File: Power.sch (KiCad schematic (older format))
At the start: 3 parts, among them P1 CONN_02X10, P2 CONN_01X05, P3 CONN_01X02

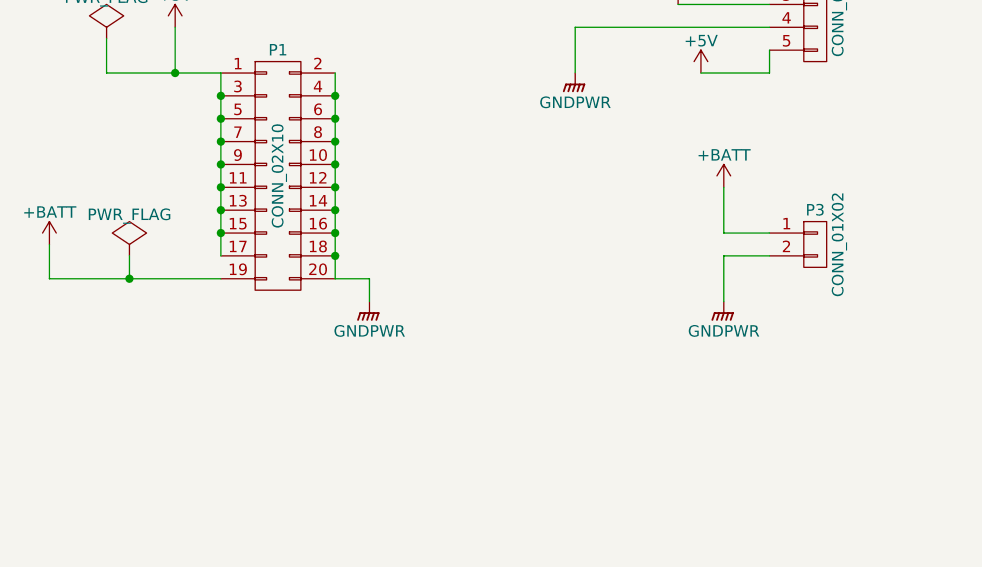
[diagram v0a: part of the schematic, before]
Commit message: Add voltage divider to pololu power
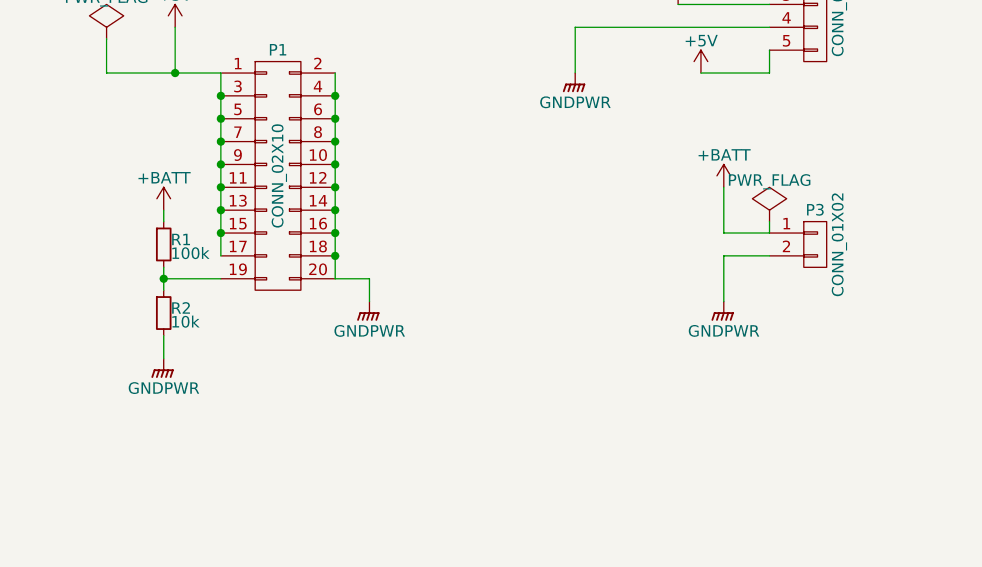
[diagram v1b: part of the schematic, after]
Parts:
- added R1: 100k, Resistors_SMD:R_0603_HandSoldering, symbol R_Small
- added R2: 10k, Resistors_SMD:R_0603_HandSoldering, symbol R_Small
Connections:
- net +BATT: now also R1.1; no longer P1.19 (P19)
- net GNDPWR: now also R2.2
- new net: P1.19 (P19), R1.2, R2.1
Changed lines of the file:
@@
 $EndComp
 $Comp
-L +BATT #PWR01
-U 1 1 56443E57
-P 650 4050
-F 0 "#PWR01" H 650 3900 50  0001 C CNN
-F 1 "+BATT" H 650 4190 50  0000 C CNN
-F 2 "" H 650 4050 60  0000 C CNN
-F 3 "" H 650 4050 60  0000 C CNN
-	1    650  4050
-	1    0    0    -1
-$EndComp
-Wire Wire Line
-	1400 4200 650  4200
-Wire Wire Line
-	650  4200 650  4050
+L GNDPWR #PWR01
+U 1 1 56443ECC
+P 2050 4300
+F 0 "#PWR01" H 2050 4100 50  0001 C CNN
+F 1 "GNDPWR" H 2050 4170 50  0000 C CNN
+F 2 "" H 2050 4250 60  0000 C CNN
+F 3 "" H 2050 4250 60  0000 C CNN
+	1    2050 4300
+	1    0    0    -1
+$EndComp
+$Comp
+L +5V #PWR02
+U 1 1 56443FAD
+P 1200 3100
+F 0 "#PWR02" H 1200 2950 50  0001 C CNN
+F 1 "+5V" H 1200 3240 50  0000 C CNN
+F 2 "" H 1200 3100 60  0000 C CNN
+F 3 "" H 1200 3100 60  0000 C CNN
+	1    1200 3100
+	1    0    0    -1
+$EndComp
+$Comp
+L PWR_FLAG #FLG03
+U 1 1 56443FC4
+P 3800 3950
+F 0 "#FLG03" H 3800 4045 50  0001 C CNN
+F 1 "PWR_FLAG" H 3800 4130 50  0000 C CNN
+F 2 "" H 3800 3950 60  0000 C CNN
+F 3 "" H 3800 3950 60  0000 C CNN
+	1    3800 3950
+	1    0    0    -1
+$EndComp
+$Comp
+L PWR_FLAG #FLG04
+U 1 1 56443FEA
+P 900 3150
+F 0 "#FLG04" H 900 3245 50  0001 C CNN
+F 1 "PWR_FLAG" H 900 3330 50  0000 C CNN
+F 2 "" H 900 3150 60  0000 C CNN
+F 3 "" H 900 3150 60  0000 C CNN
+	1    900  3150
+	1    0    0    -1
+$EndComp
+$Comp
+L CONN_01X05 P2
+U 1 1 56443F27
+P 4000 3000
+F 0 "P2" H 4000 3300 50  0000 C CNN
+F 1 "CONN_01X05" V 4100 3000 50  0000 C CNN
+F 2 "Pin_Headers:Pin_Header_Straight_1x05" H 4000 3000 60  0001 C CNN
+F 3 "" H 4000 3000 60  0000 C CNN
+	1    4000 3000
+	1    0    0    -1
+$EndComp
+$Comp
+L CONN_01X02 P3
+U 1 1 56443F4D
+P 4000 4050
+F 0 "P3" H 4000 4200 50  0000 C CNN
+F 1 "CONN_01X02" V 4100 4050 50  0000 C CNN
+F 2 "Pin_Headers:Pin_Header_Straight_1x02" H 4000 4050 60  0001 C CNN
+F 3 "" H 4000 4050 60  0000 C CNN
+	1    4000 4050
+	1    0    0    -1
+$EndComp
+$Comp
+L GNDPWR #PWR05
+U 1 1 56443FCB
+P 3600 4300
+F 0 "#PWR05" H 3600 4100 50  0001 C CNN
+F 1 "GNDPWR" H 3600 4170 50  0000 C CNN
+F 2 "" H 3600 4250 60  0000 C CNN
+F 3 "" H 3600 4250 60  0000 C CNN
+	1    3600 4300
+	1    0    0    -1
+$EndComp
+$Comp
+L GNDPWR #PWR06
+U 1 1 56444055
+P 2950 3300
+F 0 "#PWR06" H 2950 3100 50  0001 C CNN
+F 1 "GNDPWR" H 2950 3170 50  0000 C CNN
+F 2 "" H 2950 3250 60  0000 C CNN
+F 3 "" H 2950 3250 60  0000 C CNN
+	1    2950 3300
+	1    0    0    -1
+$EndComp
+$Comp
+L +BATT #PWR07
+U 1 1 56444072
+P 3400 3000
+F 0 "#PWR07" H 3400 2850 50  0001 C CNN
+F 1 "+BATT" H 3400 3140 50  0000 C CNN
+F 2 "" H 3400 3000 60  0000 C CNN
+F 3 "" H 3400 3000 60  0000 C CNN
+	1    3400 3000
+	1    0    0    -1
+$EndComp
+$Comp
+L +BATT #PWR08
+U 1 1 564440CE
+P 3600 3800
+F 0 "#PWR08" H 3600 3650 50  0001 C CNN
+F 1 "+BATT" H 3600 3940 50  0000 C CNN
+F 2 "" H 3600 3800 60  0000 C CNN
+F 3 "" H 3600 3800 60  0000 C CNN
+	1    3600 3800
+	1    0    0    -1
+$EndComp
+$Comp
+L +5V #PWR09
+U 1 1 5644412C
+P 3500 3300
+F 0 "#PWR09" H 3500 3150 50  0001 C CNN
+F 1 "+5V" H 3500 3440 50  0000 C CNN
+F 2 "" H 3500 3300 60  0000 C CNN
+F 3 "" H 3500 3300 60  0000 C CNN
+	1    3500 3300
+	1    0    0    -1
+$EndComp
+NoConn ~ 3800 2800
+NoConn ~ 3800 2900
 Wire Wire Line
 	1900 3300 1900 4200
@@
 Connection ~ 1900 4000
 Connection ~ 1900 4100
-$Comp
-L GNDPWR #PWR02
-U 1 1 56443ECC
-P 2050 4300
-F 0 "#PWR02" H 2050 4100 50  0001 C CNN
-F 1 "GNDPWR" H 2050 4170 50  0000 C CNN
-F 2 "" H 2050 4250 60  0000 C CNN
-F 3 "" H 2050 4250 60  0000 C CNN
-	1    2050 4300
-	1    0    0    -1
-$EndComp
 Wire Wire Line
 	1900 4200 2050 4200
@@
 Wire Wire Line
 	1200 3300 1200 3100
-$Comp
-L +5V #PWR03
-U 1 1 56443FAD
-P 1200 3100
-F 0 "#PWR03" H 1200 2950 50  0001 C CNN
-F 1 "+5V" H 1200 3240 50  0000 C CNN
-F 2 "" H 1200 3100 60  0000 C CNN
-F 3 "" H 1200 3100 60  0000 C CNN
-	1    1200 3100
-	1    0    0    -1
-$EndComp
-$Comp
-L PWR_FLAG #FLG04
-U 1 1 56443FC4
-P 1000 4100
-F 0 "#FLG04" H 1000 4195 50  0001 C CNN
-F 1 "PWR_FLAG" H 1000 4280 50  0000 C CNN
-F 2 "" H 1000 4100 60  0000 C CNN
-F 3 "" H 1000 4100 60  0000 C CNN
-	1    1000 4100
-	1    0    0    -1
-$EndComp
-$Comp
-L PWR_FLAG #FLG05
-U 1 1 56443FEA
-P 900 3150
-F 0 "#FLG05" H 900 3245 50  0001 C CNN
-F 1 "PWR_FLAG" H 900 3330 50  0000 C CNN
-F 2 "" H 900 3150 60  0000 C CNN
-F 3 "" H 900 3150 60  0000 C CNN
-	1    900  3150
-	1    0    0    -1
-$EndComp
 Wire Wire Line
 	900  3150 900  3300
 Connection ~ 1200 3300
 Wire Wire Line
-	1000 4100 1000 4200
-Connection ~ 1000 4200
-$Comp
-L CONN_01X05 P2
-U 1 1 56443F27
-P 4000 3000
-F 0 "P2" H 4000 3300 50  0000 C CNN
-F 1 "CONN_01X05" V 4100 3000 50  0000 C CNN
-F 2 "Pin_Headers:Pin_Header_Straight_1x05" H 4000 3000 60  0001 C CNN
-F 3 "" H 4000 3000 60  0000 C CNN
-	1    4000 3000
-	1    0    0    -1
-$EndComp
-$Comp
-L CONN_01X02 P3
-U 1 1 56443F4D
-P 4000 4050
-F 0 "P3" H 4000 4200 50  0000 C CNN
-F 1 "CONN_01X02" V 4100 4050 50  0000 C CNN
-F 2 "Pin_Headers:Pin_Header_Straight_1x02" H 4000 4050 60  0001 C CNN
-F 3 "" H 4000 4050 60  0000 C CNN
-	1    4000 4050
-	1    0    0    -1
-$EndComp
-$Comp
-L GNDPWR #PWR06
-U 1 1 56443FCB
-P 3600 4300
-F 0 "#PWR06" H 3600 4100 50  0001 C CNN
-F 1 "GNDPWR" H 3600 4170 50  0000 C CNN
-F 2 "" H 3600 4250 60  0000 C CNN
-F 3 "" H 3600 4250 60  0000 C CNN
-	1    3600 4300
-	1    0    0    -1
-$EndComp
-Wire Wire Line
 	3600 3800 3600 4000
 Wire Wire Line
@@
 	3600 4100 3600 4300
 Wire Wire Line
+	3500 3300 3800 3300
+Wire Wire Line
+	3800 3300 3800 3200
+Wire Wire Line
+	3800 3000 3400 3000
+Wire Wire Line
 	3800 3100 2950 3100
 Wire Wire Line
 	2950 3100 2950 3300
-$Comp
-L GNDPWR #PWR07
-U 1 1 56444055
-P 2950 3300
-F 0 "#PWR07" H 2950 3100 50  0001 C CNN
-F 1 "GNDPWR" H 2950 3170 50  0000 C CNN
-F 2 "" H 2950 3250 60  0000 C CNN
-F 3 "" H 2950 3250 60  0000 C CNN
-	1    2950 3300
-	1    0    0    -1
-$EndComp
-$Comp
-L +BATT #PWR08
-U 1 1 56444072
-P 3400 3000
-F 0 "#PWR08" H 3400 2850 50  0001 C CNN
-F 1 "+BATT" H 3400 3140 50  0000 C CNN
-F 2 "" H 3400 3000 60  0000 C CNN
-F 3 "" H 3400 3000 60  0000 C CNN
-	1    3400 3000
-	1    0    0    -1
-$EndComp
-Wire Wire Line
-	3500 3300 3800 3300
-Wire Wire Line
-	3800 3300 3800 3200
-$Comp
-L +BATT #PWR09
-U 1 1 564440CE
-P 3600 3800
-F 0 "#PWR09" H 3600 3650 50  0001 C CNN
-F 1 "+BATT" H 3600 3940 50  0000 C CNN
-F 2 "" H 3600 3800 60  0000 C CNN
-F 3 "" H 3600 3800 60  0000 C CNN
-	1    3600 3800
-	1    0    0    -1
-$EndComp
-Wire Wire Line
-	3800 3000 3400 3000
-$Comp
-L +5V #PWR010
-U 1 1 5644412C
-P 3500 3300
-F 0 "#PWR010" H 3500 3150 50  0001 C CNN
-F 1 "+5V" H 3500 3440 50  0000 C CNN
-F 2 "" H 3500 3300 60  0000 C CNN
-F 3 "" H 3500 3300 60  0000 C CNN
-	1    3500 3300
-	1    0    0    -1
-$EndComp
-NoConn ~ 3800 2800
-NoConn ~ 3800 2900
+Wire Wire Line
+	3800 4000 3800 3950
+$Comp
+L +BATT #PWR010
+U 1 1 56929CC6
+P 1150 3900
+F 0 "#PWR010" H 1150 3750 50  0001 C CNN
+F 1 "+BATT" H 1150 4040 50  0000 C CNN
+F 2 "" H 1150 3900 50  0000 C CNN
+F 3 "" H 1150 3900 50  0000 C CNN
+	1    1150 3900
+	1    0    0    -1
+$EndComp
+$Comp
+L R_Small R1
+U 1 1 56929CE3
+P 1150 4050
+F 0 "R1" H 1180 4070 50  0000 L CNN
+F 1 "100k" H 1180 4010 50  0000 L CNN
+F 2 "Resistors_SMD:R_0603_HandSoldering" H 1150 4050 50  0001 C CNN
+F 3 "" H 1150 4050 50  0000 C CNN
+	1    1150 4050
+	1    0    0    -1
+$EndComp
+$Comp
+L R_Small R2
+U 1 1 56929D04
+P 1150 4350
+F 0 "R2" H 1180 4370 50  0000 L CNN
+F 1 "10k" H 1180 4310 50  0000 L CNN
+F 2 "Resistors_SMD:R_0603_HandSoldering" H 1150 4350 50  0001 C CNN
+F 3 "" H 1150 4350 50  0000 C CNN
+	1    1150 4350
+	1    0    0    -1
+$EndComp
+Wire Wire Line
+	1150 3900 1150 3950
+Wire Wire Line
+	1150 4150 1150 4250
+Wire Wire Line
+	1150 4200 1400 4200
+Connection ~ 1150 4200
+$Comp
+L GNDPWR #PWR011
+U 1 1 56929DA5
+P 1150 4550
+F 0 "#PWR011" H 1150 4350 50  0001 C CNN
+F 1 "GNDPWR" H 1150 4420 50  0000 C CNN
+F 2 "" H 1150 4500 50  0000 C CNN
+F 3 "" H 1150 4500 50  0000 C CNN
+	1    1150 4550
+	1    0    0    -1
+$EndComp
+Wire Wire Line
+	1150 4550 1150 4450
 $EndSCHEMATC

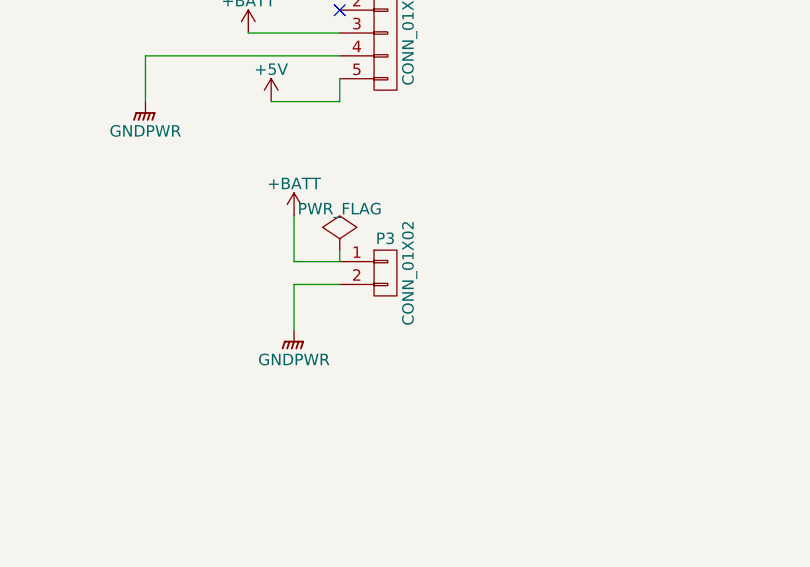
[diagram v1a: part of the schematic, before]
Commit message: v3 of pololu power. Moved pololu headers to the board edge, centered it to fit narrow standoffs, switched 5v traces to outside to hopefully strengthen the solder joint, and make annular ring of power holes larger. Thanks to Rothany Hin for breaking v2s swiftly.
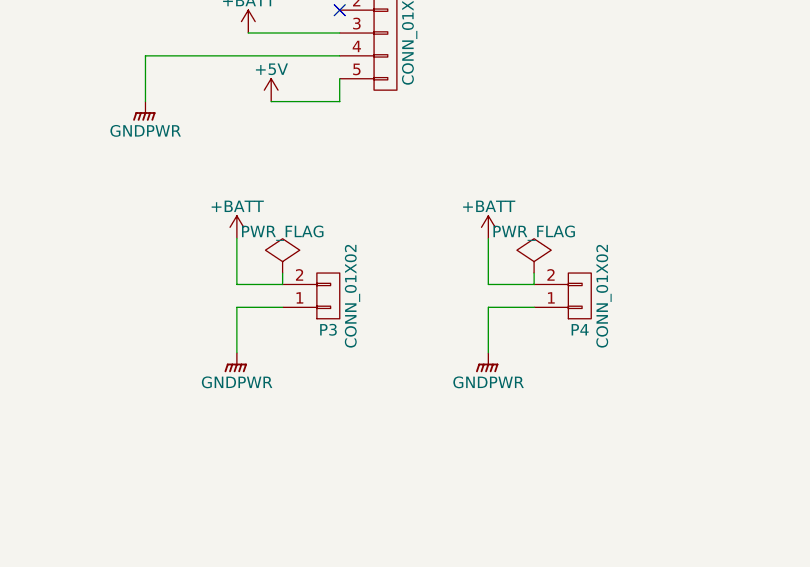
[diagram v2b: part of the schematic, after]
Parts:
- added P4: CONN_01X02, pin-headers:16awg_Pin_Header_Straight_1x02, symbol CONN_01X02
- P3: footprint Pin_Headers:Pin_Header_Straight_1x02 -> pin-headers:16awg_Pin_Header_Straight_1x02
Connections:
- net +BATT: now also P3.2 (P2), P4.2 (P2); no longer P3.1 (P1)
- net GNDPWR: now also P3.1 (P1), P4.1 (P1); no longer P3.2 (P2)
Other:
- moved on the sheet: P3
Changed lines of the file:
@@
 L PWR_FLAG #FLG03
 U 1 1 56443FC4
-P 3800 3950
-F 0 "#FLG03" H 3800 4045 50  0001 C CNN
-F 1 "PWR_FLAG" H 3800 4130 50  0000 C CNN
-F 2 "" H 3800 3950 60  0000 C CNN
-F 3 "" H 3800 3950 60  0000 C CNN
-	1    3800 3950
+P 3550 4050
+F 0 "#FLG03" H 3550 4145 50  0001 C CNN
+F 1 "PWR_FLAG" H 3550 4230 50  0000 C CNN
+F 2 "" H 3550 4050 60  0000 C CNN
+F 3 "" H 3550 4050 60  0000 C CNN
+	1    3550 4050
 	1    0    0    -1
 $EndComp
@@
 L CONN_01X02 P3
 U 1 1 56443F4D
-P 4000 4050
-F 0 "P3" H 4000 4200 50  0000 C CNN
-F 1 "CONN_01X02" V 4100 4050 50  0000 C CNN
-F 2 "Pin_Headers:Pin_Header_Straight_1x02" H 4000 4050 60  0001 C CNN
-F 3 "" H 4000 4050 60  0000 C CNN
-	1    4000 4050
-	1    0    0    -1
+P 3750 4150
+F 0 "P3" H 3750 4300 50  0000 C CNN
+F 1 "CONN_01X02" V 3850 4150 50  0000 C CNN
+F 2 "pin-headers:16awg_Pin_Header_Straight_1x02" H 3750 4150 60  0001 C CNN
+F 3 "" H 3750 4150 60  0000 C CNN
+	1    3750 4150
+	1    0    0    1
 $EndComp
 $Comp
 L GNDPWR #PWR05
 U 1 1 56443FCB
-P 3600 4300
-F 0 "#PWR05" H 3600 4100 50  0001 C CNN
-F 1 "GNDPWR" H 3600 4170 50  0000 C CNN
-F 2 "" H 3600 4250 60  0000 C CNN
-F 3 "" H 3600 4250 60  0000 C CNN
-	1    3600 4300
+P 3350 4400
+F 0 "#PWR05" H 3350 4200 50  0001 C CNN
+F 1 "GNDPWR" H 3350 4270 50  0000 C CNN
+F 2 "" H 3350 4350 60  0000 C CNN
+F 3 "" H 3350 4350 60  0000 C CNN
+	1    3350 4400
 	1    0    0    -1
 $EndComp
@@
 L +BATT #PWR08
 U 1 1 564440CE
-P 3600 3800
-F 0 "#PWR08" H 3600 3650 50  0001 C CNN
-F 1 "+BATT" H 3600 3940 50  0000 C CNN
-F 2 "" H 3600 3800 60  0000 C CNN
-F 3 "" H 3600 3800 60  0000 C CNN
-	1    3600 3800
+P 3350 3900
+F 0 "#PWR08" H 3350 3750 50  0001 C CNN
+F 1 "+BATT" H 3350 4040 50  0000 C CNN
+F 2 "" H 3350 3900 60  0000 C CNN
+F 3 "" H 3350 3900 60  0000 C CNN
+	1    3350 3900
 	1    0    0    -1
 $EndComp
@@
 Connection ~ 1200 3300
 Wire Wire Line
-	3600 3800 3600 4000
-Wire Wire Line
-	3600 4000 3800 4000
-Wire Wire Line
-	3800 4100 3600 4100
-Wire Wire Line
-	3600 4100 3600 4300
+	3350 3900 3350 4100
+Wire Wire Line
+	3350 4100 3550 4100
+Wire Wire Line
+	3550 4200 3350 4200
+Wire Wire Line
+	3350 4200 3350 4400
 Wire Wire Line
 	3500 3300 3800 3300
@@
 	2950 3100 2950 3300
 Wire Wire Line
-	3800 4000 3800 3950
+	3550 4100 3550 4050
 $Comp
 L +BATT #PWR010
@@
 Wire Wire Line
 	1150 4550 1150 4450
+$Comp
+L PWR_FLAG #FLG012
+U 1 1 56AC6DF9
+P 4650 4050
+F 0 "#FLG012" H 4650 4145 50  0001 C CNN
+F 1 "PWR_FLAG" H 4650 4230 50  0000 C CNN
+F 2 "" H 4650 4050 60  0000 C CNN
+F 3 "" H 4650 4050 60  0000 C CNN
+	1    4650 4050
+	1    0    0    -1
+$EndComp
+$Comp
+L CONN_01X02 P4
+U 1 1 56AC6DFF
+P 4850 4150
+F 0 "P4" H 4850 4300 50  0000 C CNN
+F 1 "CONN_01X02" V 4950 4150 50  0000 C CNN
+F 2 "pin-headers:16awg_Pin_Header_Straight_1x02" H 4850 4150 60  0001 C CNN
+F 3 "" H 4850 4150 60  0000 C CNN
+	1    4850 4150
+	1    0    0    1
+$EndComp
+$Comp
+L GNDPWR #PWR013
+U 1 1 56AC6E05
+P 4450 4400
+F 0 "#PWR013" H 4450 4200 50  0001 C CNN
+F 1 "GNDPWR" H 4450 4270 50  0000 C CNN
+F 2 "" H 4450 4350 60  0000 C CNN
+F 3 "" H 4450 4350 60  0000 C CNN
+	1    4450 4400
+	1    0    0    -1
+$EndComp
+$Comp
+L +BATT #PWR014
+U 1 1 56AC6E0B
+P 4450 3900
+F 0 "#PWR014" H 4450 3750 50  0001 C CNN
+F 1 "+BATT" H 4450 4040 50  0000 C CNN
+F 2 "" H 4450 3900 60  0000 C CNN
+F 3 "" H 4450 3900 60  0000 C CNN
+	1    4450 3900
+	1    0    0    -1
+$EndComp
+Wire Wire Line
+	4450 3900 4450 4100
+Wire Wire Line
+	4450 4100 4650 4100
+Wire Wire Line
+	4650 4200 4450 4200
+Wire Wire Line
+	4450 4200 4450 4400
+Wire Wire Line
+	4650 4100 4650 4050
 $EndSCHEMATC
